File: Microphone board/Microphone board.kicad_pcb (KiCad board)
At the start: 4 copper layers, 155 parts, among them J1 TF-01A, J2 OV2640, J3 NHD-2.4-240320AF-CSXP, J4 TYPE-C 16PIN 2MD(073), M1 MSM261DDB019, M10 MSM261DDB019, M11 MSM261DDB019, M12 MSM261DDB019, M13 MSM261DDB019, M14 MSM261DDB019, M15 MSM261DDB019, M16 MSM261DDB019, M2 MSM261DDB019, M3 MSM261DDB019, M4 MSM261DDB019, M5 MSM261DDB019, M6 MSM261DDB019, M7 MSM261DDB019, M8 MSM261DDB019, M9 MSM261DDB019, Q1 AO3401A, Q2 MMBT3904, U1 STM32H747XIH6, U2 24LC256, U3 TLV320ADC5140IRTWT, U4 TLV320ADC5140IRTWT, U5 TPD6F003, U6 USBLC6-2SC6, U7 AP63203WU, U8 TPS7A2033PDBV, U9 TPS2116DRL, Y1 SX2M25.000M20F30TNN

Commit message: PCB routed
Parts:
- added BT1: 3.7V 18650, Connector_Wire:SolderWire-1.5sqmm_1x02_P6mm_D1.7mm_OD3mm, F.Cu at (106.2, 135.8)
- added C75: 10u 6.3V, Capacitor_SMD:C_0805_2012Metric, F.Cu at (111.7, 130.9)
- added C76: 100n, Capacitor_SMD:C_0402_1005Metric, F.Cu at (114.2, 127.9)
- added C77: 2.2u, Capacitor_SMD:C_0402_1005Metric, F.Cu at (115.5, 118.0)
- added C78: 10u 6.3V, Capacitor_SMD:C_0805_2012Metric, F.Cu at (111.5, 122.9)
- added C79: 10u 6.3V, Capacitor_SMD:C_0805_2012Metric, F.Cu at (111.5, 124.9)
- added C80: 10u, Capacitor_SMD:C_0603_1608Metric, F.Cu at (121.8, 124.2)
- added C81: 100n, Capacitor_SMD:C_0402_1005Metric, F.Cu at (123.2, 119.5)
- added C82: 22u, Capacitor_SMD:C_0805_2012Metric, F.Cu at (126.0, 124.5)
- added C83: 22u, Capacitor_SMD:C_0805_2012Metric, F.Cu at (126.0, 126.5)
- added C84: 2.2u, Capacitor_SMD:C_0603_1608Metric, F.Cu at (115.8, 125.9)
- added C85: 2.2u, Capacitor_SMD:C_0603_1608Metric, F.Cu at (120.8, 126.9)
- added C86: 1u, Capacitor_SMD:C_0603_1608Metric, F.Cu at (101.2, 126.0)
- added C87: 1u, Capacitor_SMD:C_0603_1608Metric, F.Cu at (103.0, 130.2)
- added C88: 100n, Capacitor_SMD:C_0402_1005Metric, B.Cu at (170.0, 89.3)
- added C89: 100n, Capacitor_SMD:C_0201_0603Metric, B.Cu at (160.3, 98.4)
- added C90: OV2640, Mic_Parts:OV2640, F.Cu at (110.8, 92.2)
- added D1: Green, PCM_JLCPCB:D_0603, F.Cu at (95.0, 130.2)
- added D2: Yellow, PCM_JLCPCB:D_0603, F.Cu at (95.0, 128.8)
- added D3: Red, PCM_JLCPCB:D_0603, F.Cu at (95.0, 127.2)
- added H1: M3 mounting hole, MountingHole:MountingHole_3.2mm_M3_DIN965_Pad, F.Cu at (62.6, 42.6)
- added H2: M3 mounting hole, MountingHole:MountingHole_3.2mm_M3_DIN965_Pad, F.Cu at (62.4, 137.2)
- added H3: M3 mounting hole, MountingHole:MountingHole_3.2mm_M3_DIN965_Pad, F.Cu at (180.8, 137.2)
- added H4: M3 mounting hole, MountingHole:MountingHole_3.2mm_M3_DIN965_Pad, F.Cu at (180.8, 42.6)
- added J5: Trigger, Connector_JST:JST_PH_B2B-PH-K_1x02_P2.00mm_Vertical, F.Cu at (122.2, 136.8)
- added J6: Menu, Connector_JST:JST_PH_B6B-PH-K_1x06_P2.00mm_Vertical, F.Cu at (130.2, 136.8)
- added J7: Conn_ARM_JTAG_SWD_10, Connector_PinHeader_1.27mm:PinHeader_2x05_P1.27mm_Vertical_SMD, F.Cu at (158.0, 81.5)
- added L1: GNR4018S2R2MT, Inductor_SMD:L_Abracon_ASPI-4030S, F.Cu at (143.2, 89.0)
- added L2: GNR4018S2R2MT, Inductor_SMD:L_Abracon_ASPI-4030S, F.Cu at (107.5, 127.9)
- added L3: FNR5040S4R7MT, Inductor_SMD:L_Changjiang_FNR5040S, F.Cu at (127.0, 120.8)
- added R43: 10k, Resistor_SMD:R_0402_1005Metric, B.Cu at (170.0, 90.5)
- added R49: 100k, Resistor_SMD:R_0402_1005Metric, F.Cu at (113.0, 119.5)
- added R50: 100R, Resistor_SMD:R_0402_1005Metric, F.Cu at (114.2, 129.9)
- added R51: 10k, Resistor_SMD:R_0402_1005Metric, F.Cu at (117.0, 120.2)
- added R52: 15k, Resistor_SMD:R_0402_1005Metric, F.Cu at (118.0, 120.2)
- added R53: 470R, Resistor_SMD:R_0402_1005Metric, F.Cu at (97.5, 127.2)
- added R54: 470R, Resistor_SMD:R_0402_1005Metric, F.Cu at (97.5, 128.8)
- added R55: 470R, Resistor_SMD:R_0402_1005Metric, F.Cu at (97.2, 130.8)
- added R56: 5k1, Resistor_SMD:R_0402_1005Metric, F.Cu at (175.2, 104.4)
- added R57: 5k1, Resistor_SMD:R_0402_1005Metric, F.Cu at (175.2, 100.2)
- added R58: 22R, Resistor_SMD:R_0402_1005Metric, F.Cu at (174.3, 102.8)
- added R59: 22R, Resistor_SMD:R_0402_1005Metric, F.Cu at (174.3, 101.8)
- added R60: 1k, Resistor_SMD:R_0402_1005Metric, F.Cu at (98.2, 130.7)
- added R61: 10k, Resistor_SMD:R_0402_1005Metric, B.Cu at (148.0, 117.2)
- added R62: 10k, Resistor_SMD:R_0402_1005Metric, B.Cu at (152.0, 117.2)
- added R63: 10k, Resistor_SMD:R_0402_1005Metric, B.Cu at (151.2, 115.2)
- added R64: 10k, Resistor_SMD:R_0402_1005Metric, B.Cu at (150.4, 113.2)
- added R65: 10k, Resistor_SMD:R_0402_1005Metric, B.Cu at (149.6, 115.2)
- added R66: 10k, Resistor_SMD:R_0402_1005Metric, B.Cu at (148.8, 113.2)
- added TH1: 10k, Connector_JST:JST_PH_B2B-PH-K_1x02_P2.00mm_Vertical, F.Cu at (89.8, 131.2)
- added U10: TPS7A2033PDBV, Package_TO_SOT_SMD:SOT-23-5, F.Cu at (118.3, 126.2)
- added U11: USBLC6-2SC6, Package_TO_SOT_SMD:SOT-23-6, F.Cu at (171.2, 102.3)
- C1: value 100n -> 220pF
- C10, C11, C12, C13, C14, C16, C17, C18, C19, C20, C21, C22, C23, C24, C25, C26, C27, C8, C9: footprint Capacitor_SMD:C_0402_1005Metric -> Capacitor_SMD:C_0201_0603Metric; moved to B.Cu
- C15: value 100n -> 1u; footprint Capacitor_SMD:C_0402_1005Metric -> Capacitor_SMD:C_0603_1608Metric
- C2: footprint Capacitor_SMD:C_0402_1005Metric -> Capacitor_SMD:C_0603_1608Metric
- C28: value 4.7u -> 100n; footprint Capacitor_SMD:C_0603_1608Metric -> Capacitor_SMD:C_0201_0603Metric; moved to B.Cu
- C29: value 220pF -> 100n; footprint Capacitor_SMD:C_0402_1005Metric -> Capacitor_SMD:C_0201_0603Metric; moved to B.Cu
- C30, C31: value 10u -> 100n; footprint Capacitor_SMD:C_0805_2012Metric -> Capacitor_SMD:C_0201_0603Metric; moved to B.Cu
- C32, C33, C34: value 2.2u -> 100n; footprint Capacitor_SMD:C_0402_1005Metric -> Capacitor_SMD:C_0201_0603Metric; moved to B.Cu
- C35, C36, R1, R41, R42: moved to B.Cu
- C37: value 100n -> 4.7u; footprint Capacitor_SMD:C_0201_0603Metric -> Capacitor_SMD:C_0603_1608Metric
- C38: value 100n -> 1u; footprint Capacitor_SMD:C_0201_0603Metric -> Capacitor_SMD:C_0603_1608Metric
- C39, C40, C41, C42, C43, C44, C45, C46, C47, C48, C49, C50, C51, C52, C53, C54, C55, C56, C59, C60, C64: footprint Capacitor_SMD:C_0201_0603Metric -> Capacitor_SMD:C_0402_1005Metric
- C4, C69: value 100n -> 4.7u; footprint Capacitor_SMD:C_0402_1005Metric -> Capacitor_SMD:C_0603_1608Metric
- C57, C58, C61: value 100n -> 2.2u; footprint Capacitor_SMD:C_0201_0603Metric -> Capacitor_SMD:C_0402_1005Metric
- C6: value 100n -> 10u; footprint Capacitor_SMD:C_0402_1005Metric -> Capacitor_SMD:C_0805_2012Metric
- C62: value 4.7u -> 2.2u; footprint Capacitor_SMD:C_0603_1608Metric -> Capacitor_SMD:C_0402_1005Metric
- C63, C65: value 1u -> 100n; footprint Capacitor_SMD:C_0603_1608Metric -> Capacitor_SMD:C_0402_1005Metric
- C68: value 4.7u -> 100n; footprint Capacitor_SMD:C_0603_1608Metric -> Capacitor_SMD:C_0402_1005Metric; moved to B.Cu
- C7: value 2.2u -> 10u; footprint Capacitor_SMD:C_0402_1005Metric -> Capacitor_SMD:C_0805_2012Metric
- J1: value TF-01A -> NHD-2.4-240320AF-CSXP; footprint Mic_Parts:TF-01A -> Connector_FFC-FPC:Amphenol_F32R-1A7x1-11040_1x40-1MP_P0.5mm_Horizontal
- J2: footprint Connector_FFC-FPC:Amphenol_F32R-1A7x1-11024_1x24-1MP_P0.5mm_Horizontal -> Connector_FFC-FPC:Amphenol_F32Q-1A7x1-11024_1x24-1MP_P0.5mm_Horizontal
- J3: value NHD-2.4-240320AF-CSXP -> TF-01A; footprint Connector_FFC-FPC:Amphenol_F32R-1A7x1-11040_1x40-1MP_P0.5mm_Horizontal -> Mic_Parts:TF-01A
- Q1: value AO3401A -> MMBT3904
- Q2: value MMBT3904 -> AO3401A
- R10, R11, R12, R13, R14, R15, R16, R17, R18, R19, R20, R21, R22, R23, R24, R29, R30, R31, R32, R7, R8, R9: value 33R -> 22R
- R2: value 10k -> 2k2
- R33, R34: value 33R -> 10k
- R35: value 10k -> 1k
- R37: value 10k -> 4k7
- R38: value 10k -> 10R
- R39: value 10k -> 2R
- R4: value 2k2 -> 10k
- R44: value 10R -> 10k; moved to B.Cu
- R45: value 4k7 -> 10k; moved to B.Cu
- R46: value 2R -> 10k; moved to B.Cu
- R47: value 1k -> 10k; moved to B.Cu
- R48: value 10k -> 240k
- R5, R6: value 10k -> 22R
- U6: value USBLC6-2SC6 -> TPS63001; footprint Package_TO_SOT_SMD:SOT-23-6 -> Package_SON:Texas_DRC0010J_ThermalVias
- U7: value AP63203WU -> TPS2116DRL; footprint Package_TO_SOT_SMD:TSOT-23-6 -> Package_TO_SOT_SMD:SOT-583-8
- U8: value TPS7A2033PDBV -> AP63203WU; footprint Package_TO_SOT_SMD:SOT-23-5 -> Package_TO_SOT_SMD:TSOT-23-6
- U9: value TPS2116DRL -> MCP73833-xxx-MF; footprint Package_TO_SOT_SMD:SOT-583-8 -> Package_DFN_QFN:DFN-10-1EP_3x3mm_P0.5mm_EP1.58x2.35mm
- moved J4 125.6 mm to (180.9, 102.6), turned to 90 degrees
- moved C49 101.2 mm to (181.0, 61.5), turned to -90 degrees
- moved M1 97.5 mm to (179.0, 63.1)
- moved C32 84.0 mm to (159.7, 92.8), turned to 180 degrees
- moved C28 82.3 mm to (156.5, 92.8), turned to 180 degrees
- moved C34 82.2 mm to (151.2, 88.3), turned to -90 degrees
- moved S2 81.1 mm to (149.0, 80.2), turned to -90 degrees
- moved S1 80.4 mm to (152.5, 80.2), turned to 90 degrees
- moved C29 79.4 mm to (156.5, 94.4), turned to 180 degrees
- moved R13 79.1 mm to (177.0, 61.5), turned to -90 degrees
- moved C33 77.3 mm to (150.7, 93.6)
- moved C65 76.2 mm to (137.0, 85.7), turned to 90 degrees
- moved R4 74.9 mm to (148.5, 84.0), turned to 180 degrees
- moved C41 73.7 mm to (151.0, 72.5), turned to -90 degrees
- moved C31 73.1 mm to (159.7, 92.0), turned to 180 degrees
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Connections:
- net Net-(J4-D+-PadA6) renamed /USB/USB_IN_P
- net Net-(J4-D--PadA7) renamed /USB/USB_IN_N
- C1 pad 1: +3V3 -> Net-(U1A-VLXSMPS)
- C10 pad 1: +3V3A -> +3V3
- C12 pad 1: +3V3A -> +3V3
- C13 pad 1: +3V3A -> +3V3
- C14 pad 1: +3V3A -> +3V3
- C16 pad 1: +3V3A -> +3V3
- C17 pad 1: +3V3A -> +3V3
- C18 pad 1: +3V3A -> +3V3
- C19 pad 1: +3V3A -> +3V3
- C2 pad 1: Net-(U3B-AREG) -> Net-(U1A-VCAPDSI)
- C20 pad 1: +3V3A -> +3V3
- C21 pad 1: +3V3A -> +3V3
- C22 pad 1: +3V3A -> +3V3
- C23 pad 1: +3V3A -> +3V3
- C24 pad 1: +3V3A -> +3V3
- C27 pad 1: +3V3A -> +3V3
- C28 pad 1: Net-(U1A-VDDSMPS) -> +3V3
- C29 pad 1: Net-(U1A-VLXSMPS) -> +3V3
- C3 pad 1: Net-(U4B-AREG) -> Net-(C3-Pad1)
- C32 pad 1: Net-(C32-Pad1) -> +3V3
- C33 pad 1: Net-(C32-Pad1) -> +3V3
- C34 pad 1: Net-(U1A-VCAPDSI) -> +3V3
- C4 pad 1: Net-(U3B-VREF) -> Net-(U1A-VDDSMPS)
- C41 pad 1: +3V3 -> +3V3A
- C42 pad 1: +3V3 -> +3V3A
- C43 pad 1: +3V3 -> +3V3A
- C44 pad 1: +3V3 -> +3V3A
- C45 pad 1: +3V3 -> +3V3A
- C46 pad 1: +3V3 -> +3V3A
- C47 pad 1: +3V3 -> +3V3A
- C48 pad 1: +3V3 -> +3V3A
- C49 pad 1: +3V3 -> +3V3A
- C5 pad 1: Net-(U3B-DREG) -> Net-(C3-Pad1)
- C50 pad 1: +3V3 -> +3V3A
- C51 pad 1: +3V3 -> +3V3A
- C52 pad 1: +3V3 -> +3V3A
- C53 pad 1: +3V3 -> +3V3A
- C54 pad 1: +3V3 -> +3V3A
- C55 pad 1: +3V3 -> +3V3A
- C56 pad 1: +3V3 -> +3V3A
- C57 pad 1: +3V3 -> Net-(U3B-AREG)
- C58 pad 1: +3V3 -> Net-(U4B-AREG)
- C59 pad 1: +3V3 -> Net-(U3B-VREF)
- C6 pad 1: Net-(U4B-VREF) -> +3V3
- C60 pad 1: +3V3 -> Net-(U4B-VREF)
- C61 pad 1: +3V3 -> Net-(U3B-DREG)
- C62 pad 1: +3V3 -> Net-(U4B-DREG)
- C64 pad 1: +3V3A -> +3V3
- C66 pad 1: +3V3 -> +3V3A
- C7 pad 1: Net-(U4B-DREG) -> +3V3
- C8 pad 1: +3V3A -> +3V3
- C9 pad 1: +3V3A -> +3V3
- J1 pad 1: Net-(J1-DAT2) -> /MCU/TEAR
- J1 pad 2: Net-(J1-DAT3/CD) -> GND
- J1 pad 3: Net-(J1-CMD) -> /Display/LIGHT
- J1 pad 4: +3V3 -> GND
- J1 pad 5: Net-(J1-CLK) -> GND
- J1 pad 7: Net-(J1-DAT0) -> GND
- J1 pad 8: Net-(J1-DAT1) -> GND
- J1 pad 9: /MCU/SD_DET -> GND
- J2 pad 18: /MCU/DCMI_D7 -> /MCU/DCMI_D4
- J3 pad 1: GND -> /SD/SD_D2F
- J3 pad 2: unconnected-(J3-Pin_2-Pad2) -> /SD/SD_D3F
- J3 pad 3: unconnected-(J3-Pin_3-Pad3) -> /SD/SD_CMDF
- J3 pad 4: unconnected-(J3-Pin_4-Pad4) -> +3V3
- J3 pad 5: unconnected-(J3-Pin_5-Pad5) -> /SD/SD_CLKF
- J3 pad 6: unconnected-(J3-Pin_6-Pad6) -> GND
- J3 pad 7: +3V3 -> /SD/SD_D0F
- J3 pad 8: +3V3 -> /SD/SD_D1F
- J3 pad 9: GND -> /MCU/SD_DET
- M10 pad 4: /Microphones/CH6_CLK -> /Microphones/CH5_CLK
- M11 pad 2: GND -> +3V3A
- M11 pad 4: /Microphones/CH7_CLK -> /Microphones/CH6_CLK
- M12 pad 4: /Microphones/CH8_CLK -> /Microphones/CH6_CLK
- M13 pad 4: unconnected-(M13-CLK-Pad4) -> /Microphones/CH7_CLK
- M14 pad 2: +3V3A -> GND
- M14 pad 4: /Microphones/CH5_CLK -> /Microphones/CH7_CLK
- M15 pad 4: /Microphones/CH6_CLK -> /Microphones/CH8_CLK
- M16 pad 2: +3V3A -> GND
- M3 pad 2: GND -> +3V3A
- M4 pad 2: +3V3A -> GND
- M5 pad 2: GND -> +3V3A
- M6 pad 4: /Microphones/CH4_CLK -> /Microphones/CH3_CLK
- M7 pad 4: /Microphones/CH3_CLK -> /Microphones/CH4_CLK
- M8 pad 2: +3V3A -> GND
- M9 pad 2: GND -> +3V3A
- Q1 pad 1: Net-(Q1-G) -> Net-(Q1-B)
- Q1 pad 2: +3V3 -> GND
- Q1 pad 3: Net-(Q1-D) -> Net-(Q1-C)
- Q2 pad 1: Net-(Q2-B) -> Net-(Q2-G)
- Q2 pad 2: GND -> +3V3
- Q2 pad 3: Net-(Q2-C) -> Net-(Q2-D)
- R1 pad 1: /MCU/BOOT0 -> +3V3
- R1 pad 2: GND -> /MCU/NRST
- R10 pad 1: /Microphones/CH4_CLK -> Net-(M12-DAT)
- R10 pad 2: Net-(U3A-IN4M_GPO4) -> /Microphones/CH6_DAT
- R11 pad 1: /Microphones/CH5_CLK -> Net-(M14-DAT)
- R11 pad 2: Net-(U4A-IN1M_GPO1) -> /Microphones/CH7_DAT
- R12 pad 1: /Microphones/CH6_CLK -> Net-(M16-DAT)
- R12 pad 2: Net-(U4A-IN2M_GPO2) -> /Microphones/CH8_DAT
- R13 pad 1: /Microphones/CH7_CLK -> Net-(M1-DAT)
- R13 pad 2: Net-(U4A-IN3M_GPO3) -> /Microphones/CH1_DAT
- R14 pad 1: /Microphones/CH8_CLK -> Net-(M3-DAT)
- R14 pad 2: Net-(U4A-IN4M_GPO4) -> /Microphones/CH2_DAT
- R15 pad 1: Net-(M1-DAT) -> Net-(M5-DAT)
- R15 pad 2: /Microphones/CH1_DAT -> /Microphones/CH3_DAT
- R16 pad 1: Net-(M2-DAT) -> Net-(M7-DAT)
- R16 pad 2: /Microphones/CH1_DAT -> /Microphones/CH4_DAT
- R17 pad 1: Net-(M4-DAT) -> Net-(M9-DAT)
- R17 pad 2: /Microphones/CH2_DAT -> /Microphones/CH5_DAT
- R18 pad 1: Net-(M3-DAT) -> Net-(M11-DAT)
- R18 pad 2: /Microphones/CH2_DAT -> /Microphones/CH6_DAT
- R19 pad 1: Net-(M7-DAT) -> Net-(M13-DAT)
- R19 pad 2: /Microphones/CH3_DAT -> /Microphones/CH7_DAT
- R2 pad 2: /MCU/NRST -> /MCU/I2C4_SDA
- R20 pad 1: Net-(M5-DAT) -> Net-(M15-DAT)
- R20 pad 2: /Microphones/CH3_DAT -> /Microphones/CH8_DAT
- R21 pad 1: Net-(M8-DAT) -> /Microphones/CH5_CLK
- R21 pad 2: /Microphones/CH4_DAT -> Net-(U4A-IN1M_GPO1)
- R22 pad 1: Net-(M6-DAT) -> /Microphones/CH6_CLK
- R22 pad 2: unconnected-(R22-Pad2) -> Net-(U4A-IN2M_GPO2)
- R23 pad 1: Net-(M13-DAT) -> /Microphones/CH7_CLK
- R23 pad 2: /Microphones/CH4_DAT -> Net-(U4A-IN3M_GPO3)
- R24 pad 1: Net-(M9-DAT) -> /Microphones/CH8_CLK
- R24 pad 2: /Microphones/CH5_DAT -> Net-(U4A-IN4M_GPO4)
- R25 pad 1: Net-(M14-DAT) -> /Microphones/CH1_CLK
- R25 pad 2: /Microphones/CH5_DAT -> Net-(U3A-IN1M_GPO1)
- R26 pad 1: Net-(M10-DAT) -> /Microphones/CH2_CLK
- R26 pad 2: /Microphones/CH6_DAT -> Net-(U3A-IN2M_GPO2)
- R27 pad 1: Net-(M15-DAT) -> /Microphones/CH3_CLK
- R27 pad 2: /Microphones/CH6_DAT -> Net-(U3A-IN3M_GPO3)
- R28 pad 1: Net-(M11-DAT) -> /Microphones/CH4_CLK
- R28 pad 2: /Microphones/CH7_DAT -> Net-(U3A-IN4M_GPO4)
- R29 pad 1: Net-(M16-DAT) -> Net-(U4A-SDOUT)
- R29 pad 2: /Microphones/CH8_DAT -> Net-(U3A-GPIO1)
- R3 pad 2: /MCU/I2C4_SDA -> /MCU/I2C4_SCL
- R30 pad 1: Net-(M12-DAT) -> Net-(U3A-SDOUT)
- R30 pad 2: /Microphones/CH8_DAT -> /MCU/SAI_SD
- R31 pad 1: Net-(U3A-SDOUT) -> Net-(U3A-FSYNC)
- R31 pad 2: /MCU/SAI_SD -> /MCU/SAI_FS
- R32 pad 1: Net-(U3A-FSYNC) -> Net-(U3A-BCLK)
- R32 pad 2: /MCU/SAI_FS -> /MCU/SAI_SCK
- R33 pad 1: Net-(U3A-BCLK) -> +3V3
- R33 pad 2: /MCU/SAI_SCK -> /MCU/SHDNZ
- R34 pad 1: Net-(U4A-SDOUT) -> +3V3
- R34 pad 2: Net-(U3A-GPIO1) -> /MCU/SHDNZ
- R35 pad 1: +3V3 -> /MCU/LIGHT_PWM
- R35 pad 2: /MCU/SD_DET -> Net-(Q1-B)
- R36 pad 1: +3V3 -> GND
- R36 pad 2: Net-(J1-DAT2) -> Net-(Q1-B)
- R37 pad 1: +3V3 -> Net-(Q1-C)
- R37 pad 2: Net-(J1-DAT3/CD) -> +3V3
- R38 pad 1: +3V3 -> Net-(Q1-C)
- R38 pad 2: Net-(J1-CMD) -> Net-(Q2-G)
- R39 pad 1: +3V3 -> Net-(Q2-D)
- R39 pad 2: Net-(J1-CLK) -> /Display/LIGHT
- R4 pad 1: +3V3 -> /MCU/BOOT0
- R4 pad 2: /MCU/I2C4_SCL -> GND
- R40 pad 1: +3V3 -> GND
- R40 pad 2: Net-(J1-DAT0) -> Net-(J2-Pin_1)
- R41 pad 2: Net-(J1-DAT1) -> /SD/SD_D1F
- R42 pad 1: GND -> +3V3
- R42 pad 2: Net-(J2-Pin_1) -> /SD/SD_D0F
- R44 pad 1: Net-(Q2-C) -> +3V3
- R44 pad 2: Net-(Q1-G) -> /SD/SD_CMDF
- R45 pad 1: Net-(Q2-C) -> +3V3
- R45 pad 2: +3V3 -> /SD/SD_D3F
- R46 pad 1: Net-(Q1-D) -> +3V3
- R46 pad 2: /Display/LIGHT -> /MCU/SD_DET
- R47 pad 1: /MCU/LIGHT_PWM -> +3V3
- R47 pad 2: Net-(Q2-B) -> /SD/SD_D2F
- R48 pad 1: GND -> VBUS
- R48 pad 2: Net-(Q2-B) -> Net-(U7-PR1)
- R5 pad 1: +3V3 -> Net-(M2-DAT)
- R5 pad 2: /Microphones/SHDNZ -> /Microphones/CH1_DAT
- R6 pad 1: +3V3 -> Net-(M4-DAT)
- R6 pad 2: /Microphones/SHDNZ -> /Microphones/CH2_DAT
- R7 pad 1: /Microphones/CH1_CLK -> Net-(M6-DAT)
- R7 pad 2: Net-(U3A-IN1M_GPO1) -> /Microphones/CH3_DAT
- R8 pad 1: /Microphones/CH2_CLK -> Net-(M8-DAT)
- R8 pad 2: Net-(U3A-IN2M_GPO2) -> /Microphones/CH4_DAT
- R9 pad 1: /Microphones/CH3_CLK -> Net-(M10-DAT)
- R9 pad 2: Net-(U3A-IN3M_GPO3) -> /Microphones/CH5_DAT
- S1 pad 1: +3V3 -> /MCU/NRST
- S1 pad 2: /MCU/BOOT0 -> GND
- S2 pad 1: /MCU/NRST -> +3V3
- S2 pad 2: GND -> /MCU/BOOT0
- U1 pad A10: /MCU/DCMI_VSYNC -> unconnected-(U1D-PG9-PadA10)
- U1 pad A3: unconnected-(U1E-PI5-PadA3) -> /MCU/DCMI_VSYNC
- U1 pad A7: Net-(C32-Pad1) -> Net-(C3-Pad1)
- U1 pad B10: unconnected-(U1E-PJ15-PadB10) -> /MCU/SHDNZ
- U1 pad B14: unconnected-(U1B-SWCLK-PadB14) -> /MCU/SWCLK
- U1 pad C15: unconnected-(U1B-SWDIO-PadC15) -> /MCU/SWDIO
- U1 pad D17: Net-(C32-Pad1) -> Net-(C3-Pad1)
- U1 pad E16: /MCU/USB_DP -> /MCU/USB_P
- U1 pad E17: /MCU/USB_DM -> /MCU/USB_N
- U1 pad E7: unconnected-(U1A-PDR_ON-PadE7) -> +3V3
- U1 pad R11: unconnected-(U1D-PE15-PadR11) -> /MCU/FMC_D12
- U1 pad R6: unconnected-(U1C-PB2-PadR6) -> /MCU/SWO
- U1 pad U10: unconnected-(U1D-PE14-PadU10) -> /MCU/FMC_D11
- U1 pad U11: Net-(C32-Pad1) -> Net-(C3-Pad1)
- U1 pad U2: unconnected-(U1C-PA3-PadU2) -> /MCU/TRIGGER
- U1 pad U3: unconnected-(U1C-PA4-PadU3) -> /MCU/LEFT
- U1 pad U4: unconnected-(U1C-PC5-PadU4) -> /MCU/DOWN
- U1 pad U5: unconnected-(U1C-PB0-PadU5) -> /MCU/BUTTON
- U1 pad U6: unconnected-(U1E-PJ3-PadU6) -> /MCU/RIGHT
- U1 pad U7: unconnected-(U1E-PJ4-PadU7) -> /MCU/UP
- U3 pad 14: /Microphones/SHDNZ -> /MCU/SHDNZ
- U4 pad 14: /Microphones/SHDNZ -> /MCU/SHDNZ
- U5 pad 1: /MCU/SD_D0 -> /MCU/SD_D2
- U5 pad 10: Net-(J1-CMD) -> /SD/SD_CMDF
- U5 pad 11: Net-(J1-DAT3/CD) -> /SD/SD_D3F
- U5 pad 12: Net-(J1-DAT2) -> /SD/SD_D2F
- U5 pad 7: Net-(J1-DAT1) -> /SD/SD_D1F
- U5 pad 8: Net-(J1-DAT0) -> /SD/SD_D0F
- U5 pad 9: Net-(J1-CLK) -> /SD/SD_CLKF
- U6 pad 1: Net-(R50-Pad2) -> +5VB
- U6 pad 2: GND -> Net-(U6-L2)
- U6 pad 3: Net-(R51-Pad2) -> GND
- U6 pad 4: /MCU/USB_DP -> Net-(U6-L1)
- U6 pad 5: VBUS -> VBAT
- U6 pad 6: /MCU/USB_DM -> Net-(U6-EN)
- U7 pad 1: +3V3 -> GND
- U7 pad 3: +5V -> VBUS
- U7 pad 4: GND -> Net-(U7-PR1)
- U7 pad 5: Net-(U7-SW) -> VBUS
- U7 pad 6: Net-(U7-BST) -> +5VB
- U8 pad 1: +5V -> +3V3
- U8 pad 2: GND -> +5V
- U8 pad 4: unconnected-(U8-NC-Pad4) -> GND
- U8 pad 5: +3V3A -> Net-(U8-SW)
- U9 pad 1: GND -> VBUS
- U9 pad 2: +5V -> VBUS
- U9 pad 3: VBUS -> Net-(U9-STAT1)
- U9 pad 5: VBUS -> GND
- U9 pad 6: unconnected-(U9-VIN2-Pad6) -> Net-(U9-PROG)
- U9 pad 7: +5V -> Net-(U9-~{PG})
- U9 pad 8: /MCU/PWR_STATUS -> Net-(U9-THERM)
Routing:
- net +3V3A: track 0.00 -> 453.1 mm, vias 0 -> 35
- net VBUS: track 0.00 -> 133.0 mm, vias 0 -> 5
- net /Microphones/CH6_DAT: track 0.00 -> 94.1 mm
- net /Microphones/CH5_CLK: track 0.00 -> 85.8 mm
- net /Microphones/CH5_DAT: track 0.00 -> 84.3 mm
- net /Microphones/CH6_CLK: track 0.00 -> 79.4 mm
- net /MCU/DCMI_D1: track 0.00 -> 68.8 mm, vias 0 -> 2
- net /MCU/DCMI_D4: track 0.00 -> 68.2 mm, vias 0 -> 2
- net /MCU/DCMI_D0: track 0.00 -> 66.8 mm, vias 0 -> 2
- net /MCU/FMC_NWE: track 0.00 -> 64.3 mm, vias 0 -> 2
- net /MCU/FMC_NOE: track 0.00 -> 63.0 mm, vias 0 -> 2
- net /Microphones/CH1_CLK: track 0.00 -> 61.8 mm
- net /MCU/DCMI_HSYNC: track 0.00 -> 61.6 mm, vias 0 -> 4
- net /MCU/I2C4_SCL: track 0.00 -> 60.6 mm, vias 0 -> 5
- net /Microphones/CH1_DAT: track 0.00 -> 60.3 mm
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- added copper zone on F.Cu, net +3V3
- added copper zone on In1.Cu, net +3V3
- added copper zone on F.Cu, net +5V
- added copper zone on F.Cu, net +5VB
- added copper zone on B.Cu, net GND
- added copper zone on F.Cu, net GND
- added copper zone on In2.Cu, net GND
- added copper zone on F.Cu, net Net-(U1A-VLXSMPS)
- added copper zone on F.Cu, net Net-(U6-EN)
- added copper zone on F.Cu, net Net-(U6-L1)
- added copper zone on F.Cu, net Net-(U6-L2)
- added copper zone on F.Cu, net Net-(U8-SW)
- added copper zone on F.Cu, net VBAT
- added copper zone on F.Cu, net VBUS
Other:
- board outline added: 124.6 x 101 mm

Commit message: finished r1 of the board
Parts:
- added D4: Red, PCM_JLCPCB:D_0603, F.Cu at (126.0, 129.8)
- added D5: Red, PCM_JLCPCB:D_0603, F.Cu at (126.0, 128.2)
- added R67: 22R, Resistor_SMD:R_0402_1005Metric, B.Cu at (150.5, 86.5)
- added R68: 470R, Resistor_SMD:R_0402_1005Metric, F.Cu at (123.5, 129.8)
- added R69: 470R, Resistor_SMD:R_0402_1005Metric, F.Cu at (123.5, 128.2)
- C3, C5: footprint Capacitor_SMD:C_0402_1005Metric -> Capacitor_SMD:C_0603_1608Metric
- J1: footprint Connector_FFC-FPC:Amphenol_F32R-1A7x1-11040_1x40-1MP_P0.5mm_Horizontal -> Connector_FFC-FPC:Hirose_FH12-40S-0.5SH_1x40-1MP_P0.50mm_Horizontal
- J2: footprint Connector_FFC-FPC:Amphenol_F32Q-1A7x1-11024_1x24-1MP_P0.5mm_Horizontal -> Connector_FFC-FPC:Hirose_FH12-24S-0.5SH_1x24-1MP_P0.50mm_Horizontal
- R25, R26, R27, R28: value 33R -> 22R
- moved J1 1.05 mm to (156.5, 131.2)
- moved J2 1.04 mm to (110.8, 109.2)
- moved R15 0.90 mm to (112.8, 64.8), turned to 0 degrees
- moved C5 0.75 mm to (155.2, 104.2)
- moved C3 0.75 mm to (152.8, 84.8)
- moved H2 0.45 mm to (62.8, 137.0)
- moved H4 0.28 mm to (180.6, 42.8)
- moved H3 0.28 mm to (180.6, 137.0)
- moved H1 0.28 mm to (62.8, 42.8)
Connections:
- J1 pad 31: GND -> /MCU/FMC_NE1
- U1 pad A5: /MCU/CAM_TIM -> Net-(U1C-PB5)
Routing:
- net /MCU/PWR_STATUS: track 2.26 -> 90.3 mm, vias 1 -> 6
- net /MCU/FMC_NE1: track 0.00 -> 46.1 mm, vias 1 -> 2
- net Net-(C3-Pad1): track 4.49 -> 37.8 mm, vias 1 -> 9
- net /MCU/SD_DET: track 0.00 -> 25.7 mm, vias 2 -> 3
- net GND: track 25.7 -> 36.2 mm, vias 142 -> 1532
- net /Microphones/CH4_CLK: track 43.6 -> 53.3 mm, vias 0 -> 2
- net +5V: track 1.48 -> 6.31 mm
- net +5VB: track 0.00 -> 2.83 mm
- net /MCU/CAM_TIM: track 56.3 -> 54.3 mm, vias 2 -> 1
- net /MCU/LIGHT_PWM: track 51.3 -> 52.9 mm
- net Net-(M5-DAT): track 1.29 -> 0.00 mm
- net Net-(D5-Pad2): track 0.00 -> 1.20 mm
- net Net-(D4-Pad2): track 0.00 -> 1.20 mm
- net Net-(M8-DAT): track 0.00 -> 1.19 mm
- net Net-(U1C-PB5): track 0.00 -> 1.08 mm, vias 0 -> 1
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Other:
- board text added: "3V3"
- board text added: "5V"
- board text added: "BATT"
- board text added: "BOOT"
- board text added: "Bernard Jin"
- board text added: "CAMERA"
- board text added: "DISPLAY"
- board text added: "MENU"
- board text added: "Polyotia V1"
- board text added: "RST"
- board text added: "THERM"
- board text added: "TRIG"

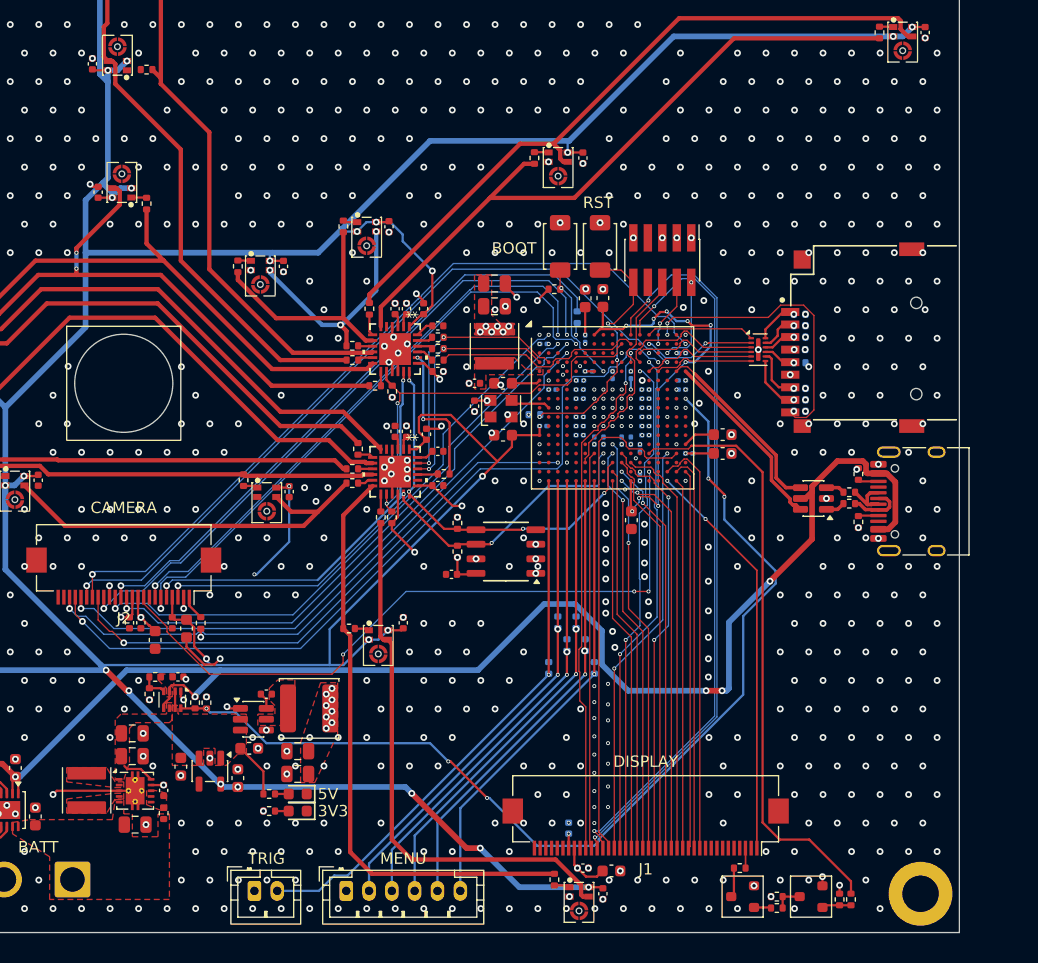
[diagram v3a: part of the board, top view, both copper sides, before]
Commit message: widened traces
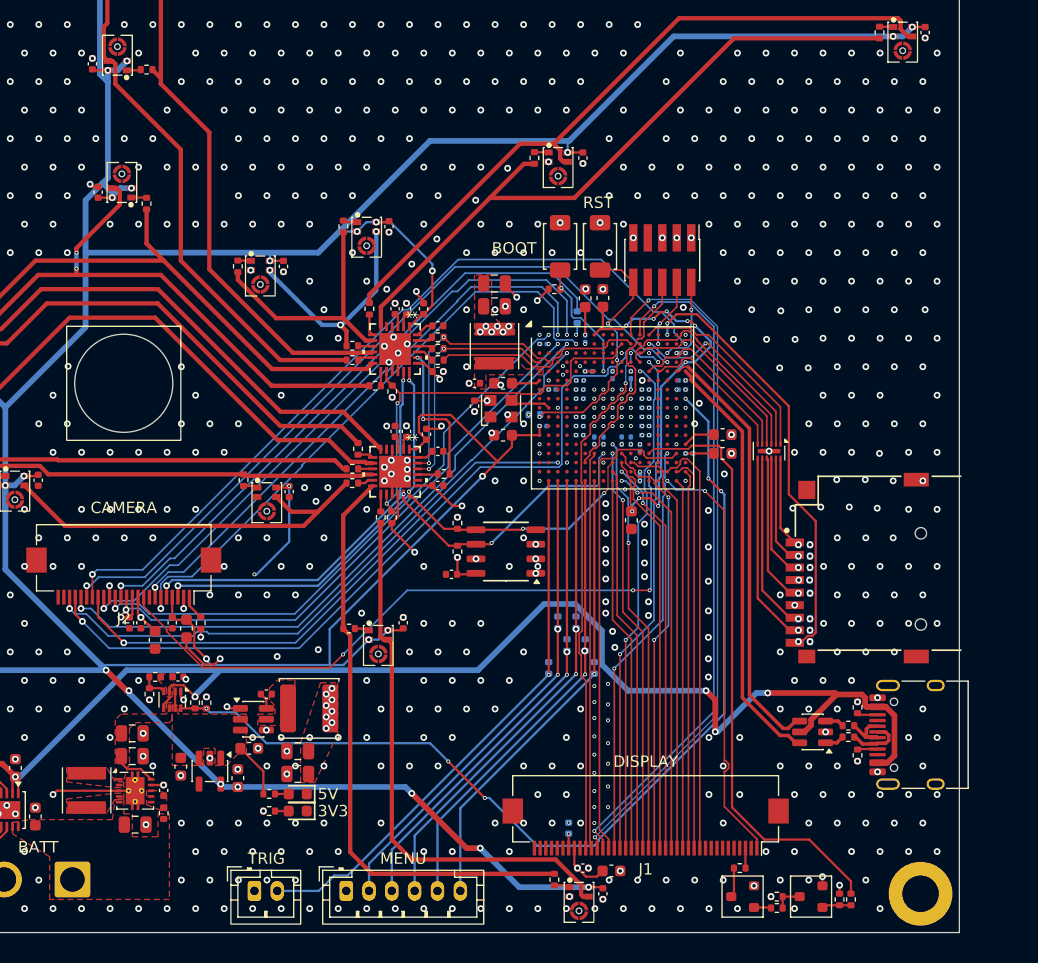
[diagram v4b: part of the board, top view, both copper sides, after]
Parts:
- moved J4 20.5 mm to (180.9, 123.1)
- moved R58 20.5 mm to (174.3, 123.3)
- moved R59 20.5 mm to (174.3, 122.3)
- moved U11 20.5 mm to (171.1, 122.8)
- moved R56 20.5 mm to (175.1, 124.9)
- moved R57 20.5 mm to (175.1, 120.7)
- moved C88 20.2 mm to (170.4, 109.5)
- moved J3 20.2 mm to (180.6, 113.4)
- moved R41 20.2 mm to (170.4, 113.9)
- moved R42 20.2 mm to (170.4, 112.9)
- moved R43 20.2 mm to (170.4, 110.7)
- moved R44 20.2 mm to (170.4, 108.4)
- moved R45 20.2 mm to (170.4, 107.4)
- moved R46 20.2 mm to (170.4, 114.9)
- moved R47 20.2 mm to (170.4, 106.4)
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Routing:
- net /MCU/USB_P: track 16.6 -> 38.0 mm
- net /MCU/USB_N: track 16.4 -> 37.3 mm
- net /MCU/SD_DET: track 25.7 -> 38.4 mm
- net /SD/SD_D1F: track 4.68 -> 16.7 mm
- net /SD/SD_D0F: track 4.39 -> 15.4 mm
- net /SD/SD_CLKF: track 2.55 -> 13.1 mm
- net /MCU/SD_D2: track 9.51 -> 17.9 mm
- net /SD/SD_CMDF: track 2.55 -> 10.7 mm
- net /MCU/SD_D3: track 9.99 -> 17.5 mm
- net /MCU/SD_CMD: track 12.7 -> 19.6 mm
- net VBUS: track 133.0 -> 126.7 mm
- net /SD/SD_D3F: track 3.15 -> 9.42 mm
- net /MCU/SD_CLK: track 10.8 -> 16.9 mm
- net /MCU/SD_D0: track 10.2 -> 15.7 mm
- net /MCU/SD_D1: track 8.81 -> 13.4 mm
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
